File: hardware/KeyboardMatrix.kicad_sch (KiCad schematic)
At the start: 172 parts

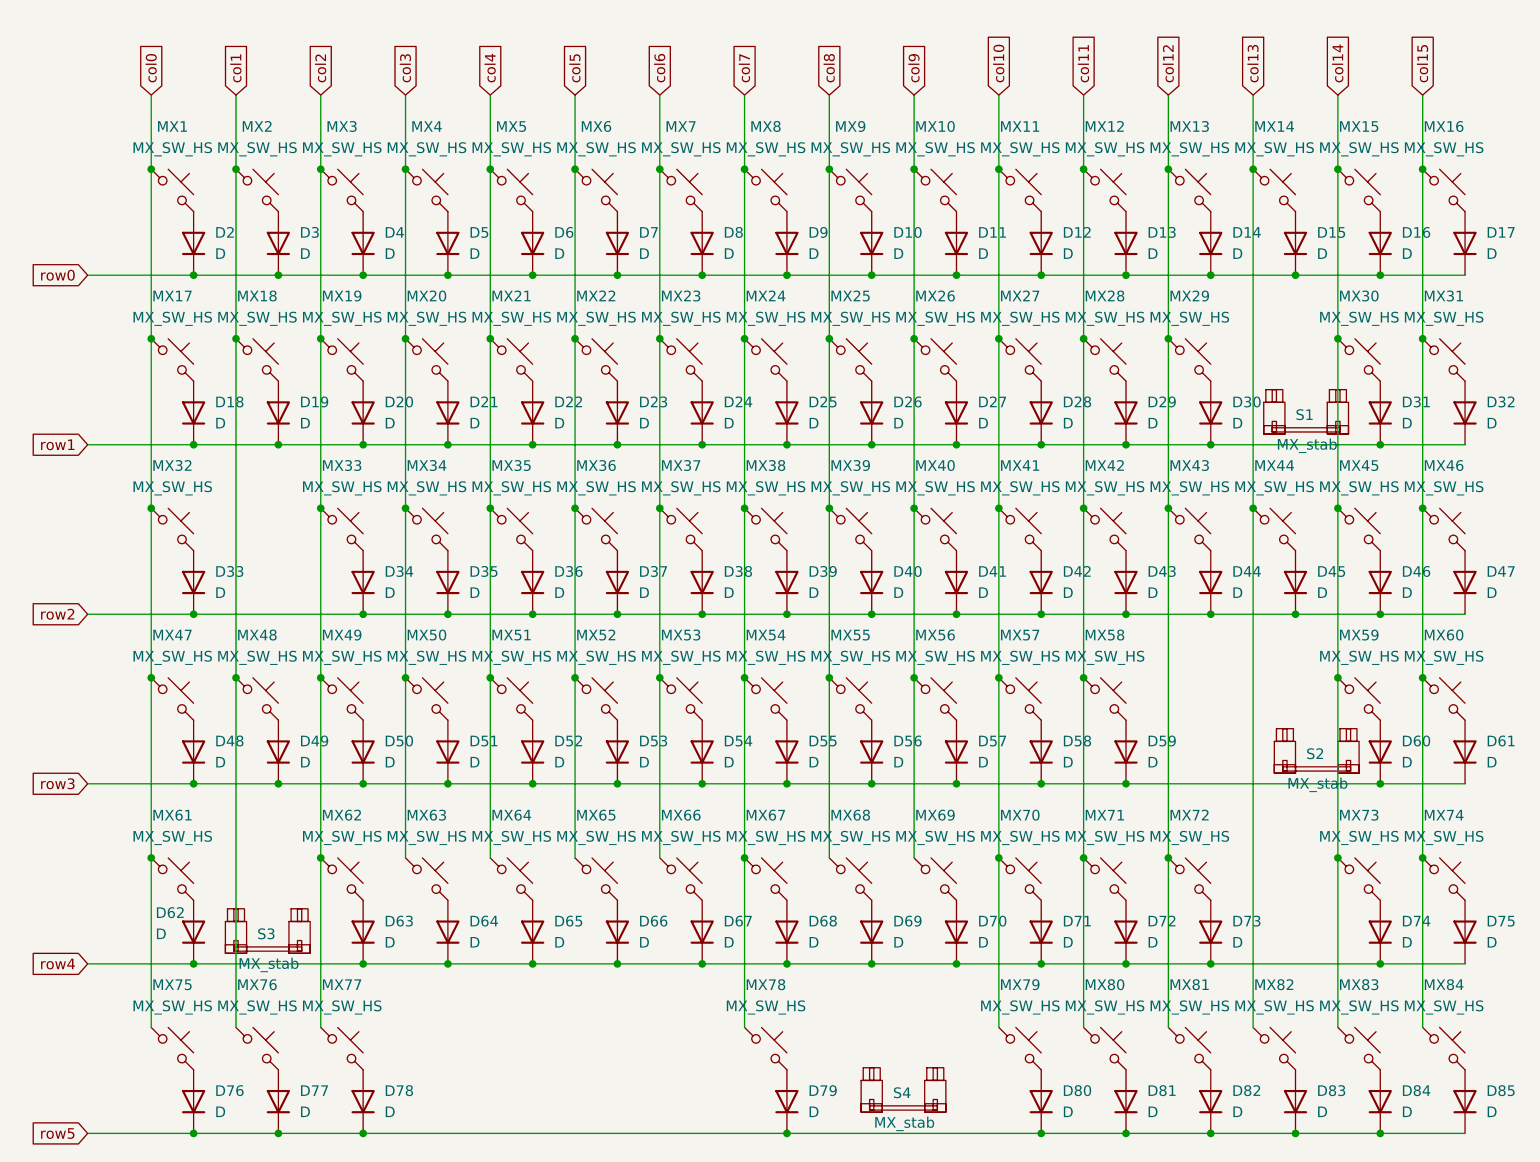
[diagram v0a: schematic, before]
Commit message: stm32layout done, started routing board
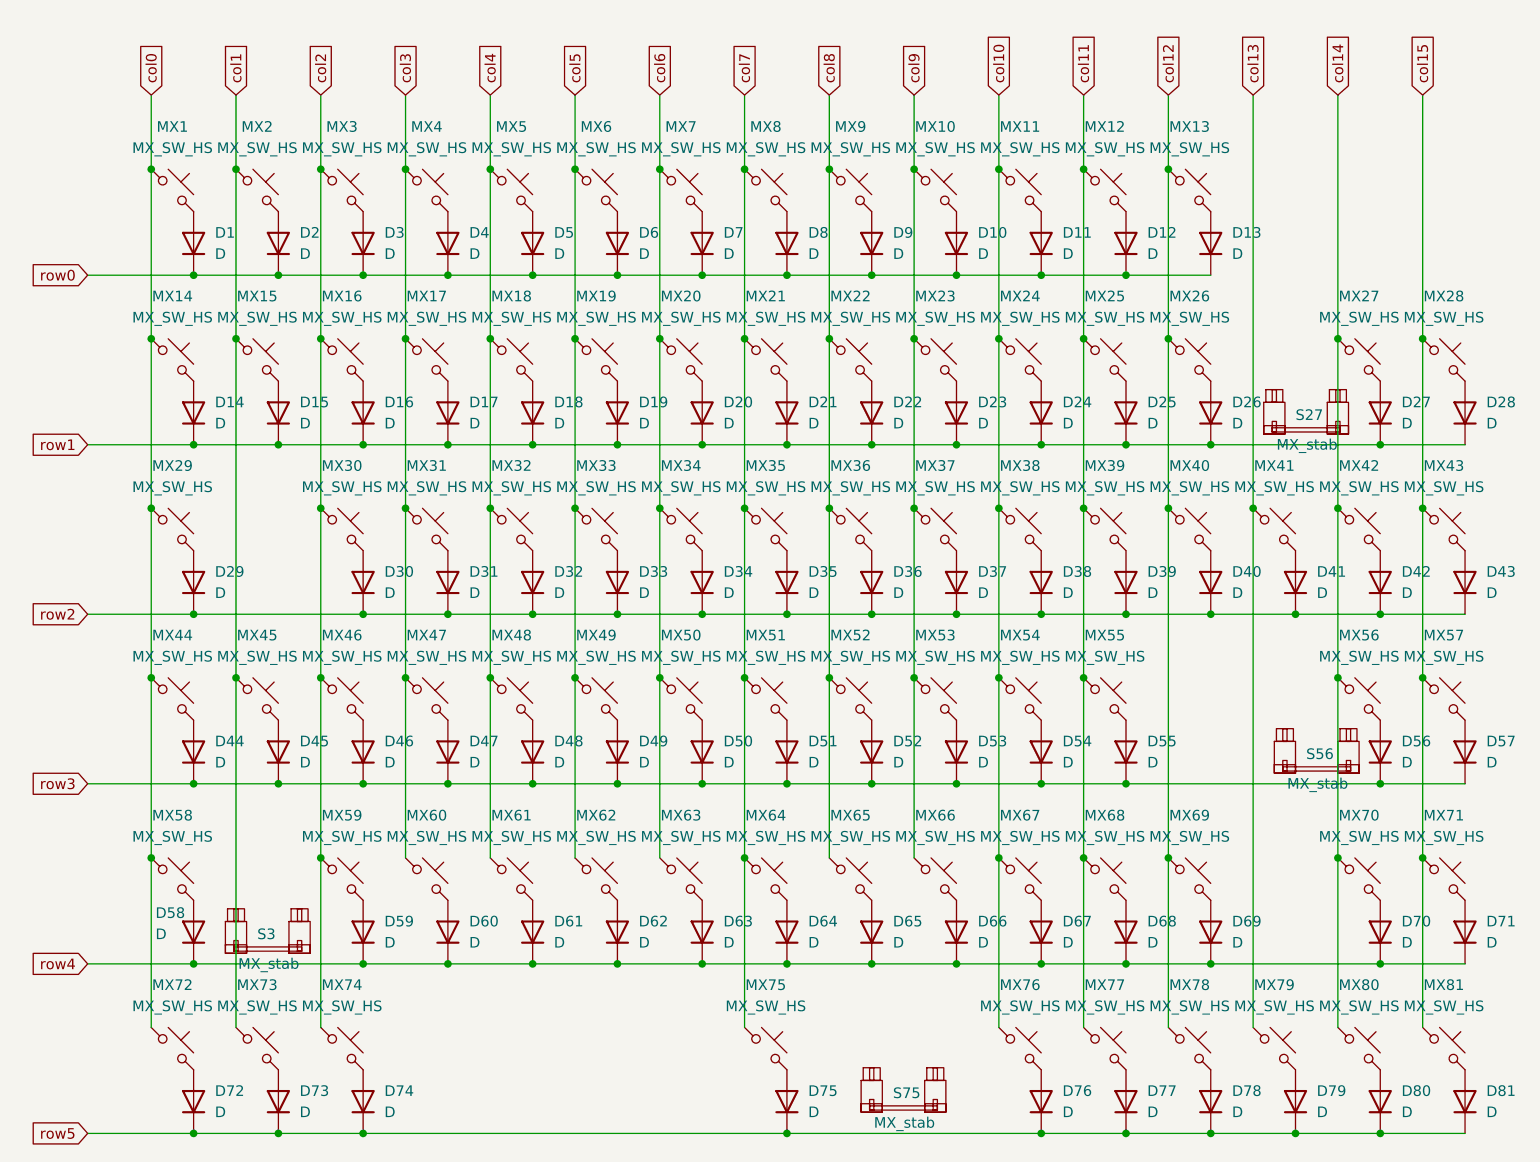
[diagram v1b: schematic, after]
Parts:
- removed D15, D16, D17: D, symbol Device:D
- removed MX14, MX15, MX16: MX_SW_HS, PCM_marbastlib-mx:SW_MX_HS_CPG151101S11_1u, symbol PCM_marbastlib-mx:MX_SW_HS_CPG151101S11
- D1: renamed from D2; footprint (none) -> Diode_SMD:D_SOD-123
- D10: renamed from D11; footprint (none) -> Diode_SMD:D_SOD-123
- D11: renamed from D12; footprint (none) -> Diode_SMD:D_SOD-123
- D12: renamed from D13; footprint (none) -> Diode_SMD:D_SOD-123
- D13: renamed from D14; footprint (none) -> Diode_SMD:D_SOD-123
- D14: renamed from D18; footprint (none) -> Diode_SMD:D_SOD-123
- D15: renamed from D19; footprint (none) -> Diode_SMD:D_SOD-123
- D16: renamed from D20; footprint (none) -> Diode_SMD:D_SOD-123
- D17: renamed from D21; footprint (none) -> Diode_SMD:D_SOD-123
- D18: renamed from D22; footprint (none) -> Diode_SMD:D_SOD-123
- D19: renamed from D23; footprint (none) -> Diode_SMD:D_SOD-123
- D2: renamed from D3; footprint (none) -> Diode_SMD:D_SOD-123
- D20: renamed from D24; footprint (none) -> Diode_SMD:D_SOD-123
- D21: renamed from D25; footprint (none) -> Diode_SMD:D_SOD-123
- D22: renamed from D26; footprint (none) -> Diode_SMD:D_SOD-123
- D23: renamed from D27; footprint (none) -> Diode_SMD:D_SOD-123
- D24: renamed from D28; footprint (none) -> Diode_SMD:D_SOD-123
- D25: renamed from D29; footprint (none) -> Diode_SMD:D_SOD-123
- D26: renamed from D30; footprint (none) -> Diode_SMD:D_SOD-123
- D27: renamed from D31; footprint (none) -> Diode_SMD:D_SOD-123
- D28: renamed from D32; footprint (none) -> Diode_SMD:D_SOD-123
- D29: renamed from D33; footprint (none) -> Diode_SMD:D_SOD-123
- D3: renamed from D4; footprint (none) -> Diode_SMD:D_SOD-123
- D30: renamed from D34; footprint (none) -> Diode_SMD:D_SOD-123
- D31: renamed from D35; footprint (none) -> Diode_SMD:D_SOD-123
- D32: renamed from D36; footprint (none) -> Diode_SMD:D_SOD-123
- D33: renamed from D37; footprint (none) -> Diode_SMD:D_SOD-123
- D34: renamed from D38; footprint (none) -> Diode_SMD:D_SOD-123
- D35: renamed from D39; footprint (none) -> Diode_SMD:D_SOD-123
- D36: renamed from D40; footprint (none) -> Diode_SMD:D_SOD-123
- D37: renamed from D41; footprint (none) -> Diode_SMD:D_SOD-123
- D38: renamed from D42; footprint (none) -> Diode_SMD:D_SOD-123
- D39: renamed from D43; footprint (none) -> Diode_SMD:D_SOD-123
- D4: renamed from D5; footprint (none) -> Diode_SMD:D_SOD-123
- D40: renamed from D44; footprint (none) -> Diode_SMD:D_SOD-123
- D41: renamed from D45; footprint (none) -> Diode_SMD:D_SOD-123
- D42: renamed from D46; footprint (none) -> Diode_SMD:D_SOD-123
- D43: renamed from D47; footprint (none) -> Diode_SMD:D_SOD-123
- D44: renamed from D48; footprint (none) -> Diode_SMD:D_SOD-123
- D45: renamed from D49; footprint (none) -> Diode_SMD:D_SOD-123
- D46: renamed from D50; footprint (none) -> Diode_SMD:D_SOD-123
- D47: renamed from D51; footprint (none) -> Diode_SMD:D_SOD-123
- D48: renamed from D52; footprint (none) -> Diode_SMD:D_SOD-123
- D49: renamed from D53; footprint (none) -> Diode_SMD:D_SOD-123
- D5: renamed from D6; footprint (none) -> Diode_SMD:D_SOD-123
- D50: renamed from D54; footprint (none) -> Diode_SMD:D_SOD-123
- D51: renamed from D55; footprint (none) -> Diode_SMD:D_SOD-123
- D52: renamed from D56; footprint (none) -> Diode_SMD:D_SOD-123
- D53: renamed from D57; footprint (none) -> Diode_SMD:D_SOD-123
- D54: renamed from D58; footprint (none) -> Diode_SMD:D_SOD-123
- D55: renamed from D59; footprint (none) -> Diode_SMD:D_SOD-123
- D56: renamed from D60; footprint (none) -> Diode_SMD:D_SOD-123
- D57: renamed from D61; footprint (none) -> Diode_SMD:D_SOD-123
- D58: renamed from D62; footprint (none) -> Diode_SMD:D_SOD-123
- D59: renamed from D63; footprint (none) -> Diode_SMD:D_SOD-123
- D6: renamed from D7; footprint (none) -> Diode_SMD:D_SOD-123
- D60: renamed from D64; footprint (none) -> Diode_SMD:D_SOD-123
- D61: renamed from D65; footprint (none) -> Diode_SMD:D_SOD-123
- D62: renamed from D66; footprint (none) -> Diode_SMD:D_SOD-123
- D63: renamed from D67; footprint (none) -> Diode_SMD:D_SOD-123
- D64: renamed from D68; footprint (none) -> Diode_SMD:D_SOD-123
- D65: renamed from D69; footprint (none) -> Diode_SMD:D_SOD-123
- D66: renamed from D70; footprint (none) -> Diode_SMD:D_SOD-123
- D67: renamed from D71; footprint (none) -> Diode_SMD:D_SOD-123
- D68: renamed from D72; footprint (none) -> Diode_SMD:D_SOD-123
- D69: renamed from D73; footprint (none) -> Diode_SMD:D_SOD-123
- D7: renamed from D8; footprint (none) -> Diode_SMD:D_SOD-123
- D70: renamed from D74; footprint (none) -> Diode_SMD:D_SOD-123
- D71: renamed from D75; footprint (none) -> Diode_SMD:D_SOD-123
- D72: renamed from D76; footprint (none) -> Diode_SMD:D_SOD-123
- D73: renamed from D77; footprint (none) -> Diode_SMD:D_SOD-123
- D74: renamed from D78; footprint (none) -> Diode_SMD:D_SOD-123
- D75: renamed from D79; footprint (none) -> Diode_SMD:D_SOD-123
- D76: renamed from D80; footprint (none) -> Diode_SMD:D_SOD-123
- D77: renamed from D81; footprint (none) -> Diode_SMD:D_SOD-123
- D78: renamed from D82; footprint (none) -> Diode_SMD:D_SOD-123
- D79: renamed from D83; footprint (none) -> Diode_SMD:D_SOD-123
- D8: renamed from D9; footprint (none) -> Diode_SMD:D_SOD-123
- D80: renamed from D84; footprint (none) -> Diode_SMD:D_SOD-123
- D81: renamed from D85; footprint (none) -> Diode_SMD:D_SOD-123
- D9: renamed from D10; footprint (none) -> Diode_SMD:D_SOD-123
- renumbered MX17 to MX14, MX18 to MX15, MX19 to MX16, MX20 to MX17, MX21 to MX18, MX22 to MX19, MX23 to MX20, MX24 to MX21, MX25 to MX22, MX26 to MX23, MX27 to MX24, MX28 to MX25, MX29 to MX26, MX30 to MX27, MX31 to MX28, MX32 to MX29, MX33 to MX30, MX34 to MX31, MX35 to MX32, MX36 to MX33, MX37 to MX34, MX38 to MX35, MX39 to MX36, MX40 to MX37, MX41 to MX38, MX42 to MX39, MX43 to MX40, MX44 to MX41, MX45 to MX42, MX46 to MX43, MX47 to MX44, MX48 to MX45, MX49 to MX46, MX50 to MX47, MX51 to MX48, MX52 to MX49, MX53 to MX50, MX54 to MX51, MX55 to MX52, MX56 to MX53, MX57 to MX54, MX58 to MX55, MX59 to MX56, MX60 to MX57, MX61 to MX58, MX62 to MX59, MX63 to MX60, MX64 to MX61, MX65 to MX62, MX66 to MX63, MX67 to MX64, MX68 to MX65, MX69 to MX66, MX70 to MX67, MX71 to MX68, MX72 to MX69, MX73 to MX70, MX74 to MX71, MX75 to MX72, MX76 to MX73, MX77 to MX74, MX78 to MX75, MX79 to MX76, MX80 to MX77, MX81 to MX78, MX82 to MX79, MX83 to MX80, MX84 to MX81, S1 to S27, S2 to S56, S4 to S75

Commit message: finished routing --> need to add test points and add i2c display. also need to request a review and refine routing.
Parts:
- S27, S3, S56: footprint PCM_marbastlib-mx:STAB_MX_P_6.25u -> PCM_marbastlib-mx:STAB_MX_P_2u
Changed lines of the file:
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@@
 			)
 		)
-		(property "Footprint" "PCM_marbastlib-mx:STAB_MX_P_6.25u"
+		(property "Footprint" "PCM_marbastlib-mx:STAB_MX_P_2u"
 			(at 74.93 129.54 0)
 			(effects
@@
 			)
 		)
-		(property "Footprint" "PCM_marbastlib-mx:STAB_MX_P_6.25u"
+		(property "Footprint" "PCM_marbastlib-mx:STAB_MX_P_2u"
 			(at 200.66 107.95 0)
 			(effects
@@
 			)
 		)
-		(property "Footprint" "PCM_marbastlib-mx:STAB_MX_P_6.25u"
+		(property "Footprint" "PCM_marbastlib-mx:STAB_MX_P_2u"
 			(at 199.39 67.31 0)
 			(effects

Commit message: added testpoints, need to readd library
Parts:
- renumbered D15 to D10, D45 to D11, D73 to D12, D3 to D13, D16 to D14, D30 to D15, D46 to D16, D59 to D17, D74 to D18, D4 to D19, D17 to D20, D31 to D21, D47 to D22, D60 to D23, D5 to D24, D18 to D25, D32 to D26, D48 to D27, D61 to D28, D6 to D29, D1 to D3, D19 to D30, D33 to D31, D49 to D32, D62 to D33, D7 to D34, D20 to D35, D34 to D36, D50 to D37, D63 to D38, D8 to D39, D14 to D4, D21 to D40, D35 to D41, D51 to D42, D64 to D43, D75 to D44, D9 to D45, D22 to D46, D36 to D47, D52 to D48, D65 to D49, D29 to D5, D10 to D50, D23 to D51, D37 to D52, D66 to D54, D11 to D55, D24 to D56, D38 to D57, D54 to D58, D67 to D59, D44 to D6, D76 to D60, D12 to D61, D25 to D62, D39 to D63, D55 to D64, D68 to D65, D77 to D66, D13 to D67, D26 to D68, D40 to D69, D58 to D7, D69 to D70, D78 to D71, D41 to D72, D79 to D73, D27 to D74, D42 to D75, D56 to D76, D70 to D77, D80 to D78, D28 to D79, D72 to D8, D43 to D80, D57 to D81, D71 to D82, D81 to D83, D2 to D9, MX73 to MX10, MX3 to MX11, MX16 to MX12, MX30 to MX13, MX46 to MX14, MX59 to MX15, MX74 to MX16, MX4 to MX17, MX17 to MX18, MX31 to MX19, MX14 to MX2, MX47 to MX20, MX60 to MX21, MX5 to MX22, MX18 to MX23, MX32 to MX24, MX48 to MX25, MX61 to MX26, MX6 to MX27, MX19 to MX28, MX33 to MX29, MX29 to MX3, MX49 to MX30, MX62 to MX31, MX7 to MX32, MX20 to MX33, MX50 to MX35, MX63 to MX36, MX8 to MX37, MX21 to MX38, MX35 to MX39, MX44 to MX4, MX51 to MX40, MX64 to MX41, MX75 to MX42, MX9 to MX43, MX22 to MX44, MX36 to MX45, MX52 to MX46, MX65 to MX47, MX10 to MX48, MX23 to MX49, MX58 to MX5, MX37 to MX50, MX53 to MX51, MX66 to MX52, MX11 to MX53, MX24 to MX54, MX38 to MX55, MX54 to MX56, MX67 to MX57, MX76 to MX58, MX12 to MX59, MX72 to MX6, MX25 to MX60, MX39 to MX61, MX55 to MX62, MX68 to MX63, MX77 to MX64, MX13 to MX65, MX26 to MX66, MX40 to MX67, MX69 to MX68, MX78 to MX69, MX2 to MX7, MX41 to MX70, MX79 to MX71, MX27 to MX72, MX42 to MX73, MX56 to MX74, MX70 to MX75, MX80 to MX76, MX28 to MX77, MX43 to MX78, MX57 to MX79, MX15 to MX8, MX71 to MX80, MX45 to MX9, S3 to S1, S75 to S2, S27 to S3, S56 to S4

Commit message: production files added --> ready for assembly
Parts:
- D1: renamed from D3; P/N (none) -> 1N4148W
- D10: renamed from D45; P/N (none) -> 1N4148W
- D11: renamed from D50; P/N (none) -> 1N4148W
- D12: renamed from D55; P/N (none) -> 1N4148W
- D13: renamed from D61; P/N (none) -> 1N4148W
- D14: renamed from D67; P/N (none) -> 1N4148W
- D15: renamed from D4; P/N (none) -> 1N4148W
- D16: renamed from D10; P/N (none) -> 1N4148W
- D17: renamed from D14; P/N (none) -> 1N4148W
- D18: renamed from D20; P/N (none) -> 1N4148W
- D19: renamed from D25; P/N (none) -> 1N4148W
- D20: renamed from D30; P/N (none) -> 1N4148W
- D21: renamed from D35; P/N (none) -> 1N4148W
- D22: renamed from D40; P/N (none) -> 1N4148W
- D23: renamed from D46; P/N (none) -> 1N4148W
- D24: renamed from D51; P/N (none) -> 1N4148W
- D25: renamed from D56; P/N (none) -> 1N4148W
- D26: renamed from D62; P/N (none) -> 1N4148W
- D27: renamed from D68; P/N (none) -> 1N4148W
- D28: renamed from D74; P/N (none) -> 1N4148W
- D29: renamed from D79; P/N (none) -> 1N4148W
- D3: renamed from D9; P/N (none) -> 1N4148W
- D30: renamed from D5; P/N (none) -> 1N4148W
- D31: renamed from D15; P/N (none) -> 1N4148W
- D32: renamed from D21; P/N (none) -> 1N4148W
- D33: renamed from D26; P/N (none) -> 1N4148W
- D34: renamed from D31; P/N (none) -> 1N4148W
- D35: renamed from D36; P/N (none) -> 1N4148W
- D36: renamed from D41; P/N (none) -> 1N4148W
- D37: renamed from D47; P/N (none) -> 1N4148W
- D38: renamed from D52; P/N (none) -> 1N4148W
- D39: renamed from D57; P/N (none) -> 1N4148W
- D4: renamed from D13; P/N (none) -> 1N4148W
- D40: renamed from D63; P/N (none) -> 1N4148W
- D41: renamed from D69; P/N (none) -> 1N4148W
- D42: renamed from D72; P/N (none) -> 1N4148W
- D43: renamed from D75; P/N (none) -> 1N4148W
- D44: renamed from D80; P/N (none) -> 1N4148W
- D45: renamed from D6; P/N (none) -> 1N4148W
- D46: renamed from D11; P/N (none) -> 1N4148W
- D47: renamed from D16; P/N (none) -> 1N4148W
- D48: renamed from D22; P/N (none) -> 1N4148W
- D49: renamed from D27; P/N (none) -> 1N4148W
- D5: renamed from D19; P/N (none) -> 1N4148W
- D50: renamed from D32; P/N (none) -> 1N4148W
- D51: renamed from D37; P/N (none) -> 1N4148W
- D52: renamed from D42; P/N (none) -> 1N4148W
- D53: renamed from D48; P/N (none) -> 1N4148W
- D54: renamed from D53; P/N (none) -> 1N4148W
- D55: renamed from D58; P/N (none) -> 1N4148W
- D56: renamed from D64; P/N (none) -> 1N4148W
- D57: renamed from D76; P/N (none) -> 1N4148W
- D58: renamed from D81; P/N (none) -> 1N4148W
- D59: renamed from D7; P/N (none) -> 1N4148W
- D6: renamed from D24; P/N (none) -> 1N4148W
- D60: renamed from D17; P/N (none) -> 1N4148W
- D61: renamed from D23; P/N (none) -> 1N4148W
- D62: renamed from D28; P/N (none) -> 1N4148W
- D63: renamed from D33; P/N (none) -> 1N4148W
- D64: renamed from D38; P/N (none) -> 1N4148W
- D65: renamed from D43; P/N (none) -> 1N4148W
- D66: renamed from D49; P/N (none) -> 1N4148W
- D67: renamed from D54; P/N (none) -> 1N4148W
- D68: renamed from D59; P/N (none) -> 1N4148W
- D69: renamed from D65; P/N (none) -> 1N4148W
- D7: renamed from D29; P/N (none) -> 1N4148W
- D70: P/N (none) -> 1N4148W
- D71: renamed from D77; P/N (none) -> 1N4148W
- D72: renamed from D82; P/N (none) -> 1N4148W
- D73: renamed from D8; P/N (none) -> 1N4148W
- D74: renamed from D12; P/N (none) -> 1N4148W
- D75: renamed from D18; P/N (none) -> 1N4148W
- D76: renamed from D44; P/N (none) -> 1N4148W
- D77: renamed from D60; P/N (none) -> 1N4148W
- D78: renamed from D66; P/N (none) -> 1N4148W
- D79: renamed from D71; P/N (none) -> 1N4148W
- D8: renamed from D34; P/N (none) -> 1N4148W
- D80: renamed from D73; P/N (none) -> 1N4148W
- D81: renamed from D78; P/N (none) -> 1N4148W
- D82: renamed from D83; P/N (none) -> 1N4148W
- D9: renamed from D39; P/N (none) -> 1N4148W
- renumbered MX48 to MX10, MX53 to MX11, MX59 to MX12, MX65 to MX13, MX2 to MX14, MX8 to MX15, MX12 to MX16, MX18 to MX17, MX23 to MX18, MX28 to MX19, MX7 to MX2, MX33 to MX20, MX38 to MX21, MX44 to MX22, MX49 to MX23, MX54 to MX24, MX60 to MX25, MX66 to MX26, MX72 to MX27, MX77 to MX28, MX3 to MX29, MX11 to MX3, MX13 to MX30, MX19 to MX31, MX24 to MX32, MX29 to MX33, MX39 to MX35, MX45 to MX36, MX50 to MX37, MX55 to MX38, MX61 to MX39, MX17 to MX4, MX67 to MX40, MX70 to MX41, MX73 to MX42, MX78 to MX43, MX4 to MX44, MX9 to MX45, MX14 to MX46, MX20 to MX47, MX25 to MX48, MX30 to MX49, MX22 to MX5, MX35 to MX50, MX40 to MX51, MX46 to MX52, MX51 to MX53, MX56 to MX54, MX62 to MX55, MX74 to MX56, MX79 to MX57, MX5 to MX58, MX15 to MX59, MX27 to MX6, MX21 to MX60, MX26 to MX61, MX31 to MX62, MX36 to MX63, MX41 to MX64, MX47 to MX65, MX52 to MX66, MX57 to MX67, MX63 to MX68, MX68 to MX69, MX32 to MX7, MX75 to MX70, MX80 to MX71, MX6 to MX72, MX10 to MX73, MX16 to MX74, MX42 to MX75, MX58 to MX76, MX64 to MX77, MX69 to MX78, MX71 to MX79, MX37 to MX8, MX76 to MX80, MX43 to MX9, S3 to S1, S4 to S2, S1 to S3, S2 to S4
